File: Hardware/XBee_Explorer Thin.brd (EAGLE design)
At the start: 45.7 x 54.6 mm, 129 parts, among them J4 QWIIC_RIGHT_ANGLE, Q2 3.1A/30V/105mΩ, U1 FSUSB30MUX_MSOP10, U2 AP63203, U3 ESD Diode, U5 ESD Diode, U6 CP210X

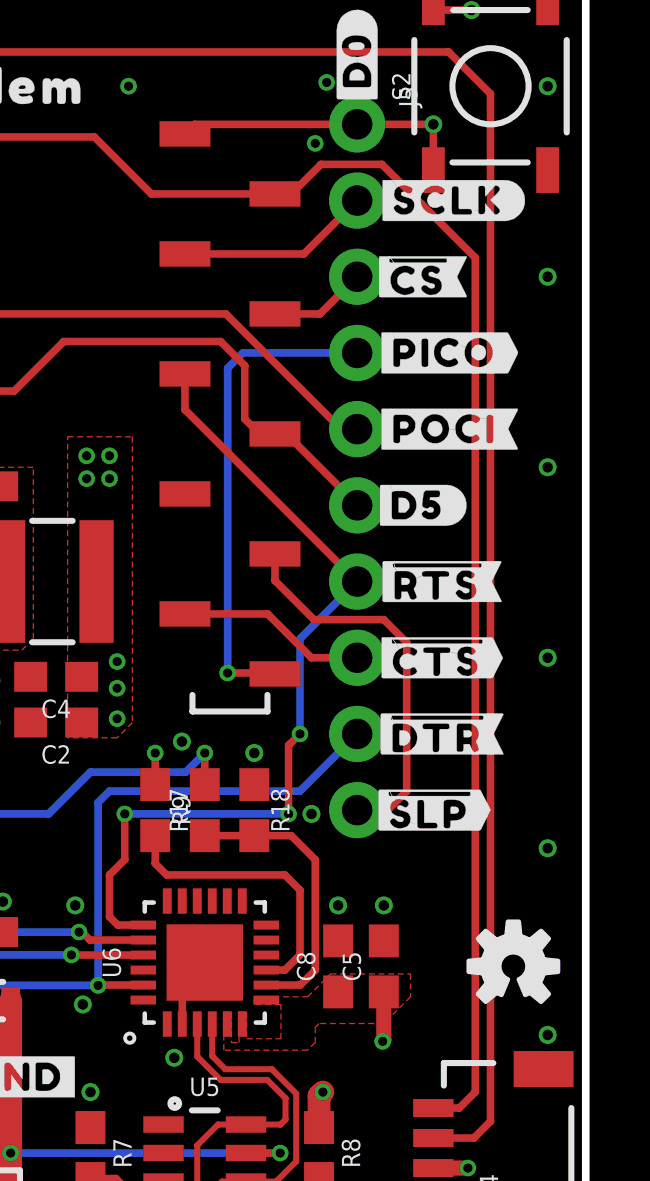
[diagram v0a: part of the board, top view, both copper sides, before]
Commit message: Moves some silk labels, approves some DRC
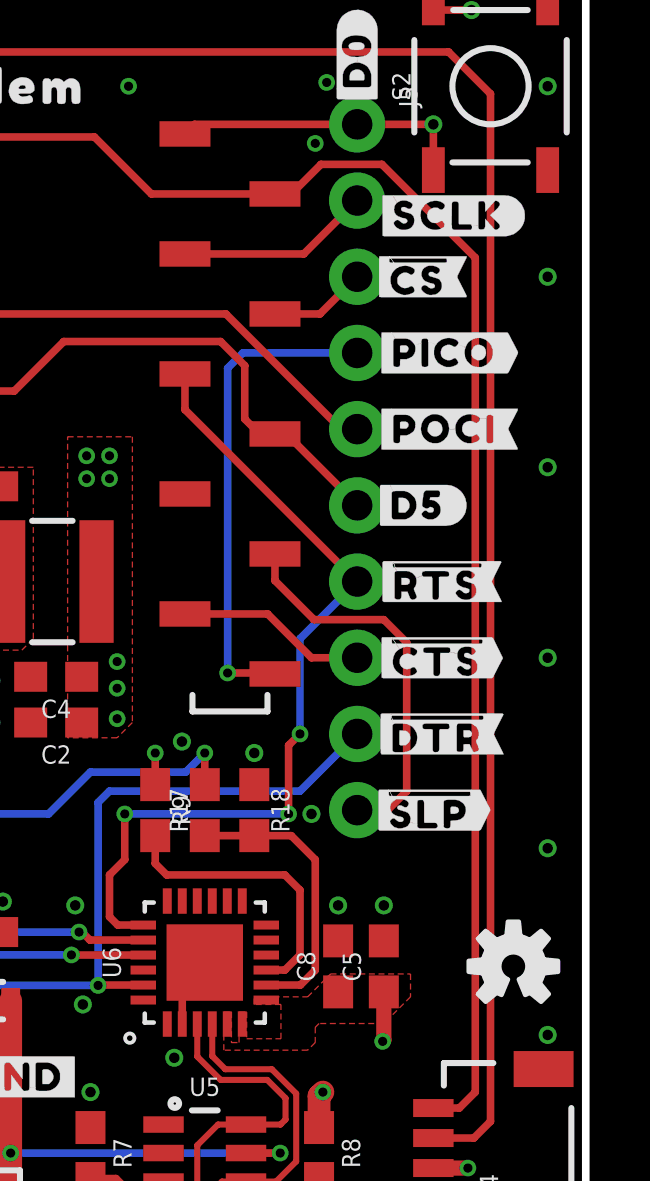
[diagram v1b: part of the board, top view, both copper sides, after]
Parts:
- moved U$33 0.51 mm to (39.9, 41.4)
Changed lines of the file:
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@@
 <element name="U$31" library="top" package="#RSSI#16" value="" x="3.556" y="36.83" smashed="yes"/>
 <element name="U$32" library="top" package="#SCL#6" value="" x="3.937" y="31.75" smashed="yes"/>
-<element name="U$33" library="top" package="#SCLK#18" value="" x="39.878" y="41.91" smashed="yes"/>
+<element name="U$33" library="top" package="#SCLK#18" value="" x="39.878" y="41.402" smashed="yes"/>
 <element name="U$34" library="top" package="#SDA#7" value="" x="3.683" y="29.21" smashed="yes"/>
 <element name="U$35" library="top" package="#SHLD#30" value="" x="32.512" y="3.429" smashed="yes" rot="MR0"/>
@@
 </polygon>
 <wire x1="39.37" y1="9.66" x2="40.521" y2="9.66" width="0.508" layer="1"/>
-<wire x1="37.68" y1="15.494" x2="37.719" y2="15.533" width="0.508" layer="1"/>
 <wire x1="13.68" y1="17.383" x2="12.716" y2="17.383" width="0.254" layer="1"/>
 <wire x1="12.716" y1="17.383" x2="12.573" y2="17.526" width="0.254" layer="1"/>

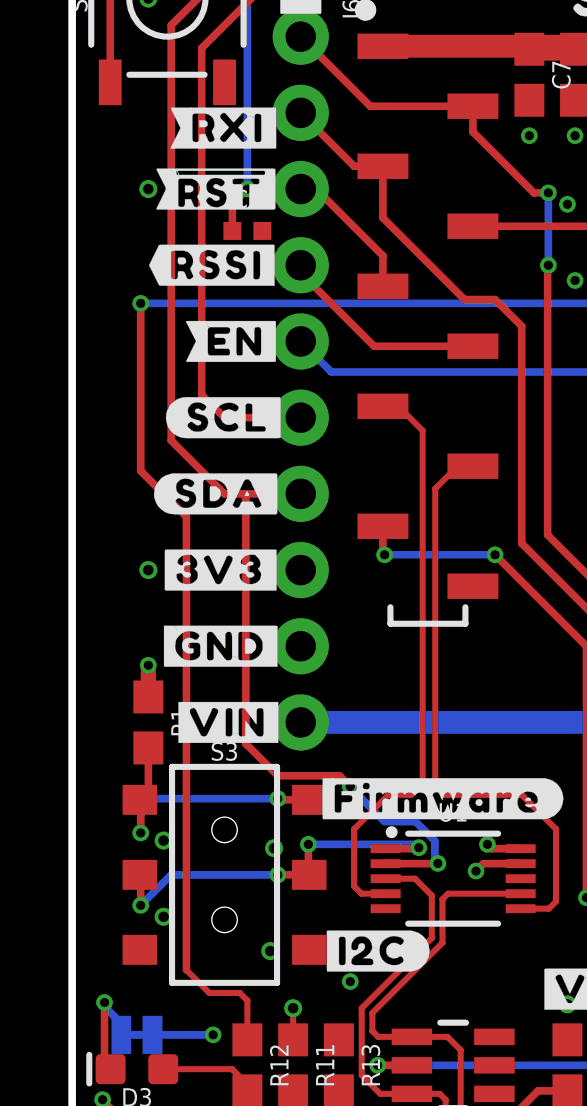
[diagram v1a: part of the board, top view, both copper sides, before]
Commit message: Adds a few more stitching vias
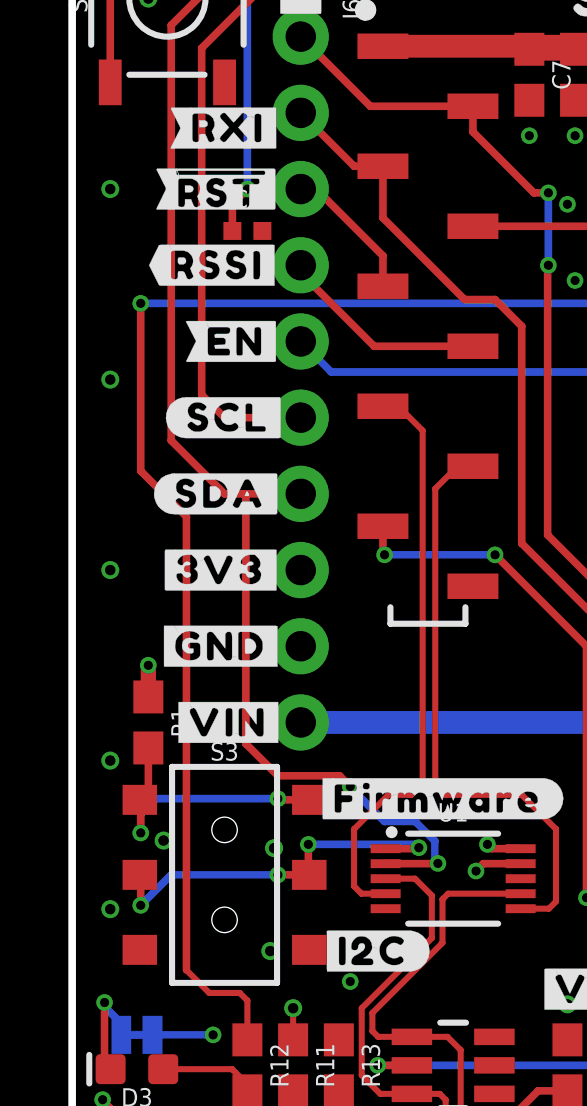
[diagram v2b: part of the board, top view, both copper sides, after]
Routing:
- net GND: vias 54 -> 56
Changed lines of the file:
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@@
 <via x="5.334" y="13.97" extent="1-16" drill="0.35"/>
 <via x="5.461" y="17.399" extent="1-16" drill="0.35"/>
-<via x="1.778" y="15.113" extent="1-16" drill="0.35"/>
 <via x="1.778" y="17.653" extent="1-16" drill="0.35"/>
 <via x="18.161" y="19.939" extent="1-16" drill="0.35"/>
@@
 <via x="43.18" y="14.097" extent="1-16" drill="0.35"/>
 <via x="1.27" y="45.72" extent="1-16" drill="0.35"/>
-<via x="1.27" y="39.37" extent="1-16" drill="0.35"/>
-<via x="1.27" y="26.67" extent="1-16" drill="0.35"/>
 <via x="13.97" y="53.34" extent="1-16" drill="0.3048"/>
 <via x="21.59" y="53.34" extent="1-16" drill="0.3048"/>
@@
 <via x="26.67" y="3.81" extent="1-16" drill="0.3048"/>
 <via x="16.51" y="3.81" extent="1-16" drill="0.3048"/>
+<via x="0" y="39.37" extent="1-16" drill="0.35"/>
+<via x="0" y="33.02" extent="1-16" drill="0.35"/>
+<via x="0" y="26.67" extent="1-16" drill="0.35"/>
+<via x="0" y="20.32" extent="1-16" drill="0.35"/>
+<via x="0" y="15.367" extent="1-16" drill="0.35"/>
 </signal>
 <signal name="3.3V">

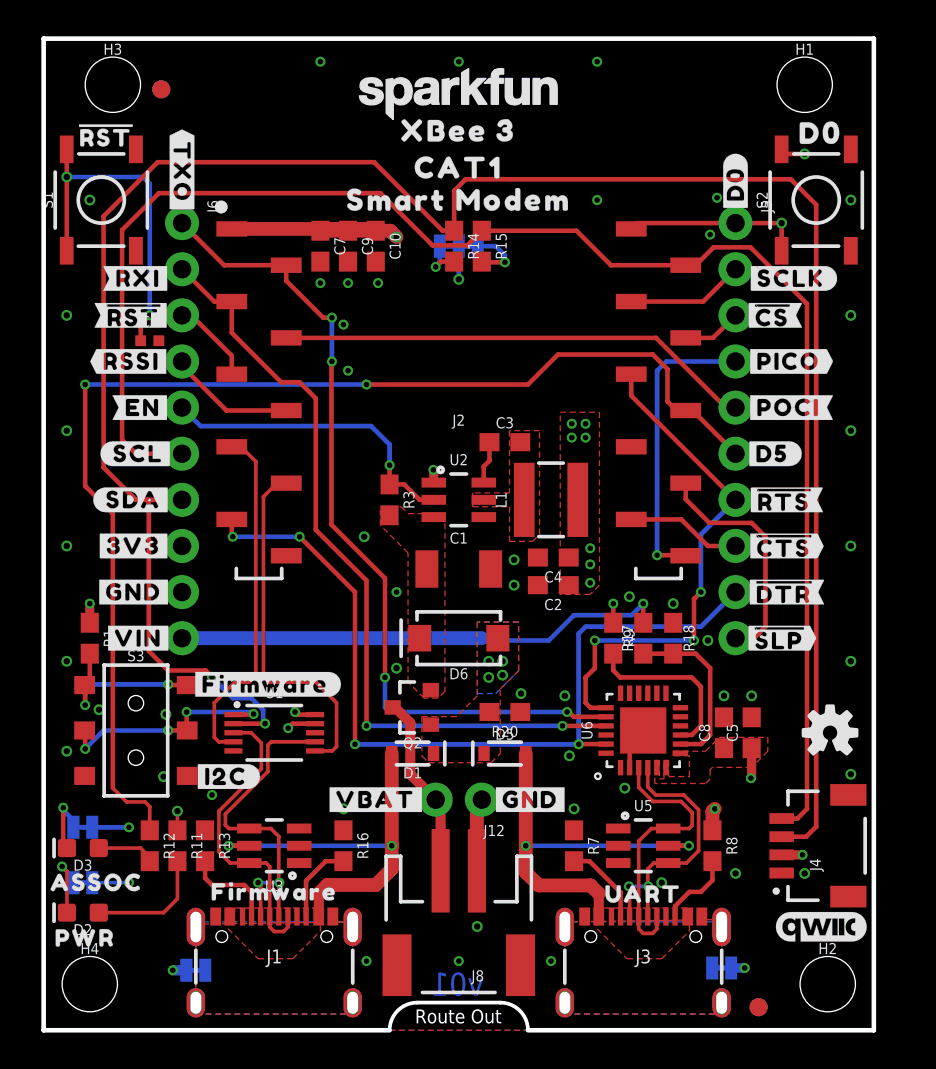
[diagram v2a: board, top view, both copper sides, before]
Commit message: Runs the correct DRC with four layers
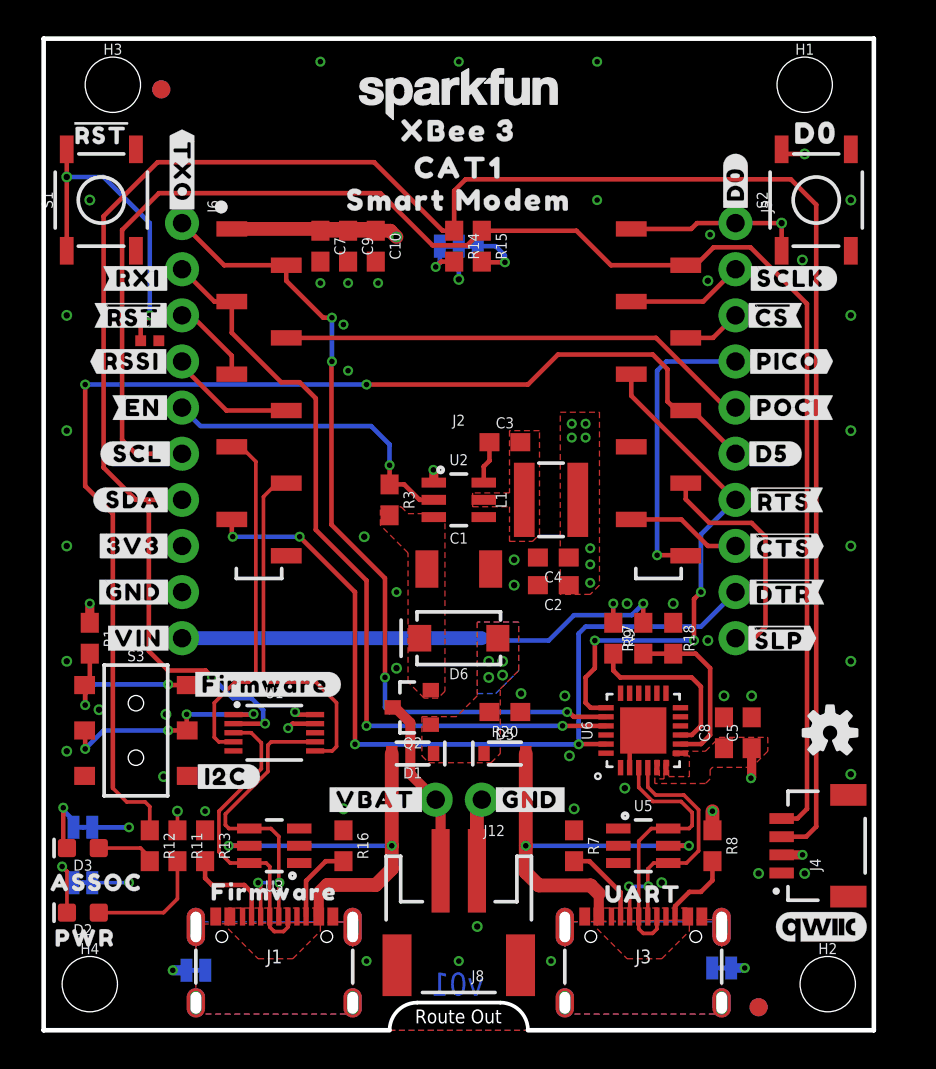
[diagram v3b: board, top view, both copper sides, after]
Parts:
- moved U$30 0.28 mm to (1.91, 49.4)
- moved U$40 0.25 mm to (41.3, 49.4)
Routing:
- net !RESET!: track 25.6 -> 24.4 mm
- net GND: track 14.8 -> 14.6 mm, vias 56 -> 57
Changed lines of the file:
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@@
 <element name="U$8" library="top" package="FIRMWARE29" value="" x="11.43" y="7.62" smashed="yes"/>
 <element name="U$49" library="bot" package="#I2C#31" value="" x="8.763" y="13.97" smashed="yes"/>
-<element name="U$40" library="bot" package="D03" value="" x="41.529" y="49.403" smashed="yes"/>
+<element name="U$40" library="bot" package="D03" value="" x="41.275" y="49.403" smashed="yes"/>
 <element name="U$50" library="top" package="#TXO#12" value="" x="6.35" y="47.244" smashed="yes" rot="R270"/>
 <element name="U$1" library="top" package="#RXI#14" value="" x="3.937" y="41.402" smashed="yes"/>
@@
 <element name="U$48" library="bot" package="#FIRMWARE#31" value="" x="10.922" y="19.05" smashed="yes"/>
 <element name="U$65" library="top" package="UART32" value="" x="31.75" y="7.493" smashed="yes"/>
-<element name="U$30" library="top" package="#RST#30" value="" x="2.159" y="49.276" smashed="yes"/>
+<element name="U$30" library="top" package="#RST#30" value="" x="1.905" y="49.403" smashed="yes"/>
 <element name="U$63" library="SparkFun-Aesthetics" package="SFE_LOGO_NAME_.2" value="" x="21.59" y="49.53" smashed="yes" rot="MR0"/>
 </elements>
@@
 <via x="18.161" y="24.13" extent="1-16" drill="0.3048"/>
 <wire x1="35.56" y1="11.01" x2="35.56" y2="12.065" width="0.762" layer="1"/>
-<wire x1="35.56" y1="12.065" x2="35.687" y2="12.192" width="0.762" layer="1"/>
-<via x="35.687" y="12.192" extent="1-16" drill="0.3048"/>
+<via x="35.56" y="12.065" extent="1-16" drill="0.3048"/>
 <contactref element="J6" pad="9"/>
 <via x="13.97" y="41.148" extent="1-16" drill="0.3048"/>
 <via x="29.21" y="53.34" extent="1-16" drill="0.3048"/>
 <wire x1="6.5913" y1="3.302" x2="5.842" y2="3.302" width="0.5588" layer="16"/>
-<via x="8.001" y="12.954" extent="1-16" drill="0.3048"/>
+<via x="7.62" y="12.065" extent="1-16" drill="0.3048"/>
 <wire x1="1.4097" y1="8.128" x2="3.429" y2="8.128" width="0.2032" layer="16"/>
 <via x="3.429" y="8.128" extent="1-16" drill="0.3048"/>
@@
 <via x="27.94" y="12.192" extent="1-16" drill="0.35"/>
 <via x="40.64" y="8.636" extent="1-16" drill="0.35"/>
-<via x="36.83" y="8.636" extent="1-16" drill="0.35"/>
+<via x="38.1" y="8.636" extent="1-16" drill="0.35"/>
 <via x="15.24" y="12.192" extent="1-16" drill="0.35"/>
 <via x="5.334" y="13.97" extent="1-16" drill="0.35"/>
@@
 <via x="15.494" y="36.322" extent="1-16" drill="0.3048"/>
 <via x="30.734" y="13.335" extent="1-16" drill="0.35"/>
-<via x="30.988" y="23.876" extent="1-16" drill="0.35"/>
+<via x="30.861" y="23.495" extent="1-16" drill="0.35"/>
 <via x="22.606" y="5.715" extent="1-16" drill="0.35"/>
 <via x="36.195" y="18.415" extent="1-16" drill="0.35"/>
@@
 <via x="35.306" y="21.463" extent="1-16" drill="0.35"/>
 <via x="29.21" y="45.72" extent="1-16" drill="0.3048"/>
-<via x="35.814" y="45.847" extent="1-16" drill="0.3048"/>
 <via x="35.433" y="43.815" extent="1-16" drill="0.3048"/>
 <via x="43.18" y="45.72" extent="1-16" drill="0.35"/>
@@
 <via x="0" y="20.32" extent="1-16" drill="0.35"/>
 <via x="0" y="15.367" extent="1-16" drill="0.35"/>
+<via x="40.513" y="42.418" extent="1-16" drill="0.35"/>
+<via x="35.306" y="41.275" extent="1-16" drill="0.35"/>
 </signal>
 <signal name="3.3V">
@@
 <via x="4.572" y="39.37" extent="1-16" drill="0.3048"/>
 <wire x1="0" y1="46.99" x2="0" y2="42.926" width="0.254" layer="1"/>
-<wire x1="4.572" y1="39.37" x2="4.572" y2="46.609" width="0.254" layer="16"/>
+<wire x1="4.572" y1="44.45" x2="4.572" y2="39.37" width="0.254" layer="16"/>
 <contactref element="J6" pad="3"/>
 <wire x1="6.35" y1="39.37" x2="4.572" y2="39.37" width="0.254" layer="16"/>
@@
 <wire x1="4.072" y1="38.87" x2="4.572" y2="39.37" width="0.254" layer="1"/>
 <via x="0" y="46.99" extent="1-16" drill="0.35"/>
-<wire x1="4.572" y1="46.609" x2="4.191" y2="46.99" width="0.254" layer="16"/>
-<wire x1="4.191" y1="46.99" x2="0" y2="46.99" width="0.254" layer="16"/>
+<wire x1="4.572" y1="44.45" x2="2.032" y2="46.99" width="0.254" layer="16"/>
+<wire x1="2.032" y1="46.99" x2="0" y2="46.99" width="0.254" layer="16"/>
 </signal>
 <signal name="D10/RSSI_PWM">
@@
 <wire x1="39.37" y1="42.926" x2="39.37" y2="44.45" width="0.254" layer="1"/>
 <contactref element="J2" pad="20"/>
-<wire x1="31.09" y1="44.13" x2="31.41" y2="44.45" width="0.254" layer="1"/>
-<wire x1="31.41" y1="44.45" x2="36.83" y2="44.45" width="0.254" layer="1"/>
+<wire x1="34.712" y1="44.45" x2="34.392" y2="44.13" width="0.254" layer="1"/>
+<wire x1="31.09" y1="44.13" x2="34.392" y2="44.13" width="0.254" layer="1"/>
+<wire x1="34.712" y1="44.45" x2="36.83" y2="44.45" width="0.254" layer="1"/>
 <wire x1="36.83" y1="44.45" x2="39.37" y2="44.45" width="0.254" layer="1"/>
 <via x="39.37" y="44.45" extent="1-16" drill="0.35"/>
-<wire x1="39.37" y1="44.45" x2="39.37" y2="46.99" width="0.254" layer="15"/>
-<wire x1="39.37" y1="46.99" x2="40.64" y2="48.26" width="0.254" layer="15"/>
+<wire x1="39.37" y1="44.45" x2="39.37" y2="47.244" width="0.254" layer="15"/>
+<wire x1="40.386" y1="48.26" x2="39.37" y2="47.244" width="0.254" layer="15"/>
+<wire x1="40.386" y1="48.26" x2="40.64" y2="48.26" width="0.254" layer="15"/>
 <via x="40.64" y="48.26" extent="1-16" drill="0.35"/>
 <wire x1="39.37" y1="48.514" x2="39.624" y2="48.26" width="0.254" layer="1"/>
@@
 <wire x1="9.18" y1="17.383" x2="10.287" y2="17.383" width="0.254" layer="1"/>
 <via x="10.287" y="17.4164" extent="1-16" drill="0.3048"/>
-<wire x1="10.287" y1="17.4164" x2="10.1774" y2="17.526" width="0.254" layer="16"/>
-<wire x1="10.1774" y1="17.526" x2="6.604" y2="17.526" width="0.254" layer="16"/>
-<via x="6.604" y="17.526" extent="1-16" drill="0.3048"/>
-<wire x1="6.604" y1="17.526" x2="6.604" y2="16.764" width="0.254" layer="1"/>
+<wire x1="10.287" y1="17.4164" x2="10.2696" y2="17.399" width="0.254" layer="16"/>
+<wire x1="10.2696" y1="17.399" x2="6.604" y2="17.399" width="0.254" layer="16"/>
+<via x="6.604" y="17.399" extent="1-16" drill="0.3048"/>
+<wire x1="6.604" y1="17.399" x2="6.604" y2="16.764" width="0.254" layer="1"/>
 <wire x1="6.604" y1="16.764" x2="6.35" y2="16.51" width="0.254" layer="1"/>
 <wire x1="6.635" y1="16.51" x2="5.588" y2="16.51" width="0.254" layer="1"/>
